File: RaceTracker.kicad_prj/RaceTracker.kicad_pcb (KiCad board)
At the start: 4 copper layers, 117 x 107.4 mm, 134 parts, among them J1 USB-C Sink, J10 MicroSD, J11 e-Paper (steckbar, Debug), J12 SWD-Programmierheader, J7 LiPo, Q1 2N7002, Q2 SIA817, Q3 2N7002, Q5 BSS138PS, U1 D21G18, U103 ZED-F9P RTK GNSS, U2 NINA-W102, U3 AP2112K-3.3 -> +3V3D, U5 BQ24195L, U6 AP2112K-3.3 -> +3V3, U7 MPU-6050 (I2C 0x68), Y1 32768Hz

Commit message: Routing: 93,8% automatisch via FreeRouting geroutet, Branding ergänzt
Specctra-DSN-Export der platzierten Platine → FreeRouting (Open-Source-
Autorouter, headless über kicad-cli/pcbnew-API-Pipeline) → SES-Re-Import.
20 Durchläufe, 388 → 24 unverdrahtete Verbindungen (93,8% Autoroute-Quote).
Verbleibende 24 sind größtenteils feinstufige QFN-Pins von U1 (SAMD21)
und U2 (NINA-W102) — brauchen manuelles Fine-Pitch-Routing, für das ich
ohne visuelle Kontrolle keine verlässliche automatische Lösung anbieten
kann.

Silkscreen-Branding auf der Rückseite ergänzt: Name "Jona Schramm -
Objectix Software Solutions" als Text sowie das Objectix-Logo, aus der
bereitgestellten PNG-Datei in ca. 440 gefüllte Silkscreen-Rechtecke
rasterisiert (0,15mm Zellgröße, 18x12mm) — plottet damit korrekt in
echte Fertigungs-Gerber-Dateien, anders als KiCads "Referenzbild"-
Funktion, die rein editor-intern bleibt.

Board auf 117x125mm erweitert (unterer Streifen für das Branding).

Verbleibende DRC-Meldungen (497, davon 29 unverdrahtet): größtenteils
Silkscreen-Kosmetik (Übersplitterung, Textgröße) ohne elektrische
Relevanz, plus dieselben ~5 Sub-Millimeter-Präzisionsartefakte aus der
bewährten Eagle-Spenderplatine wie zuvor dokumentiert.

Co-Authored-By: Claude Sonnet 5 <noreply@anthropic.com>
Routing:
- net GND: track 0.00 -> 720.4 mm, vias 0 -> 7
- net +3V3: track 0.00 -> 377.8 mm, vias 0 -> 13
- net I2C_SCL: track 0.00 -> 208.4 mm, vias 0 -> 9
- net I2C_SDA: track 0.00 -> 175.1 mm, vias 0 -> 6
- net SD_CS: track 0.00 -> 129.5 mm, vias 0 -> 4
- net LED_FIX: track 0.00 -> 127.2 mm, vias 0 -> 3
- net SPI_MOSI: track 0.00 -> 97.1 mm, vias 0 -> 1
- net EPD_RST: track 0.00 -> 96.8 mm, vias 0 -> 1
- net EPD_CS: track 0.00 -> 87.7 mm, vias 0 -> 2
- net Net-(U103-V_BKCP): track 0.00 -> 77.2 mm, vias 0 -> 2
- net IMU_INT: track 0.00 -> 76.6 mm, vias 0 -> 3
- net Net-(J10-DAT2): track 0.00 -> 72.9 mm, vias 0 -> 2
- net /Power/+3V8: track 0.00 -> 69.9 mm, vias 0 -> 6
- net SPI_MISO: track 0.00 -> 68.4 mm, vias 0 -> 3
- net Net-(U103-TIMEPULSE): track 0.00 -> 60.5 mm, vias 0 -> 2
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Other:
- board size 117 x 107.4 mm -> 117 x 125.4 mm
- board text added: "Design: Jona Schramm - Objectix Software Solutions"

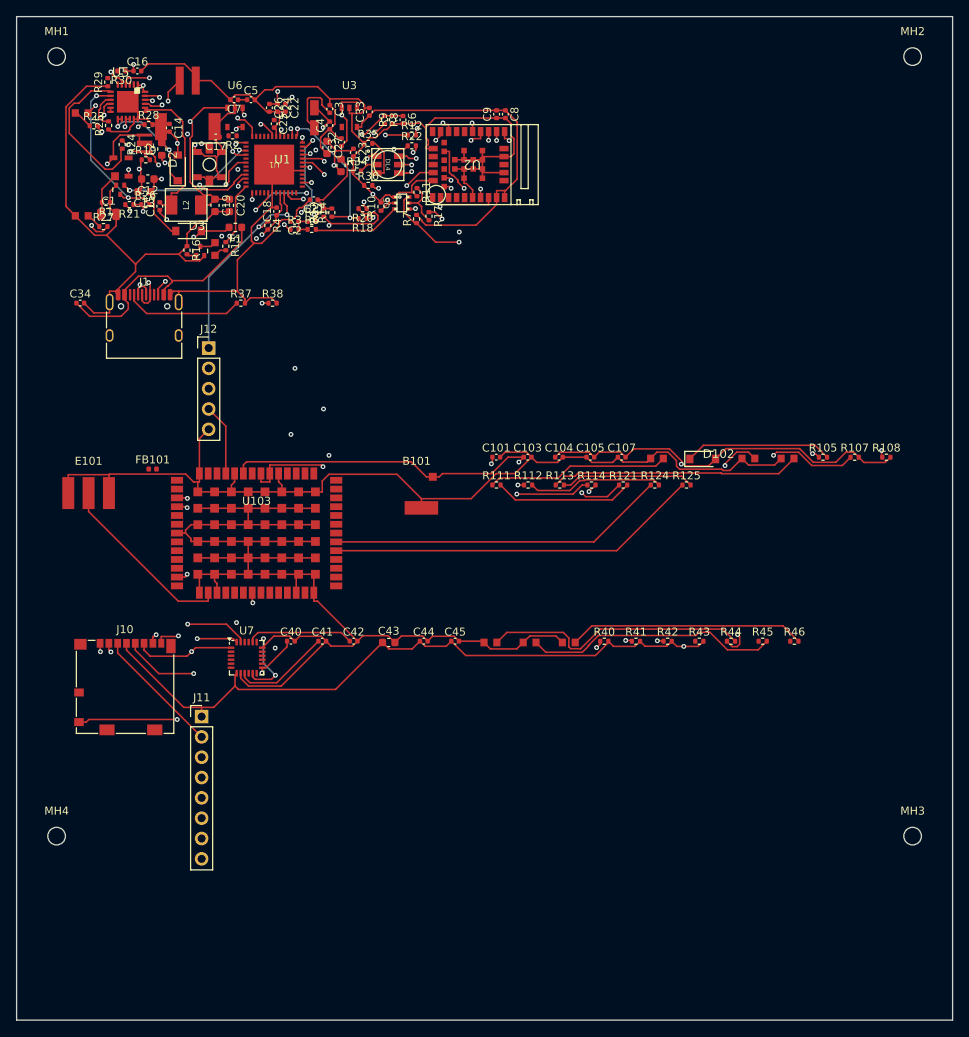
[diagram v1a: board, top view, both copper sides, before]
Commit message: PCB-Layout finalisiert: Edge-Connectoren, RF-Cluster restauriert, Routing 92,8%
- USB-C (J1), MicroSD (J10) und GPS-Antenne (E101) bündig an derselben
  Gehäusekante platziert, korrekt nach außen orientiert (90°, empirisch
  gegen pcbnew's CW-Rotationskonvention verifiziert). Akku-Stecker (J7)
  bleibt bewusst im Gehäuseinneren.
- GPS-RF-Cluster (E101/U103/FB101) nach versehentlicher manueller
  Verschiebung wieder auf die u-blox-Referenzabstände gebracht; Board
  wuchs dafür gezielt nur an der Oberkante (+15mm), keine Breitenzunahme.
- Fehlende Courtyard-Definition bei ZED_F9P_LGA102 ergänzt (verdeckte
  Überlappungen mit einem Dutzend Bauteilen, die DRC vorher nicht sah).
- Eagle-Import-Artefakte bereinigt: fehlplatzierte Ursprungsmarker auf
  8 Footprints (F.CrtYd -> F.Fab) behoben unclosed-courtyard-Fehler;
  verirrtes Mask-Polygon auf QFN48 behoben flächendeckende
  Solder-Mask-Bridge-Fehler zwischen allen Pin-Paaren.
  Solder_mask_margin auf beiden QFN-Footprints (48/24-Pin) auf 0 gesetzt,
  da 0.1016mm bei 0.5mm-Pitch die Maskenstege fast auflöste.
  Q2-Footprint (SON65P205X205X75-8N-MWSD): Pad-Größen leicht verkleinert,
  da einzelne Pads bei 0.65mm-Pitch 0mm Abstand hatten.
- Alle übrigen Platzierungskonflikte (Courtyard-Overlaps, Shorts durch
  Pad-Nähe) über iterativen Multi-Body-Relaxations-Solver aufgelöst.
- FreeRouting: 360/388 Netze (92,8%) automatisch geroutet, 4-lagig.
  Copper-edge-clearance-Regel auf 0.15mm gesetzt (realistischer Fab-Wert,
  vorher 0.5mm nicht erreichbar direkt an den bündigen Edge-Connectoren).
- Ergebnis: 0 DRC-Fehler (nur kosmetische Silk-Warnings), 0 ERC-Fehler,
  28 Netze für manuelles Routing offen.

Co-Authored-By: Claude Sonnet 5 <noreply@anthropic.com>
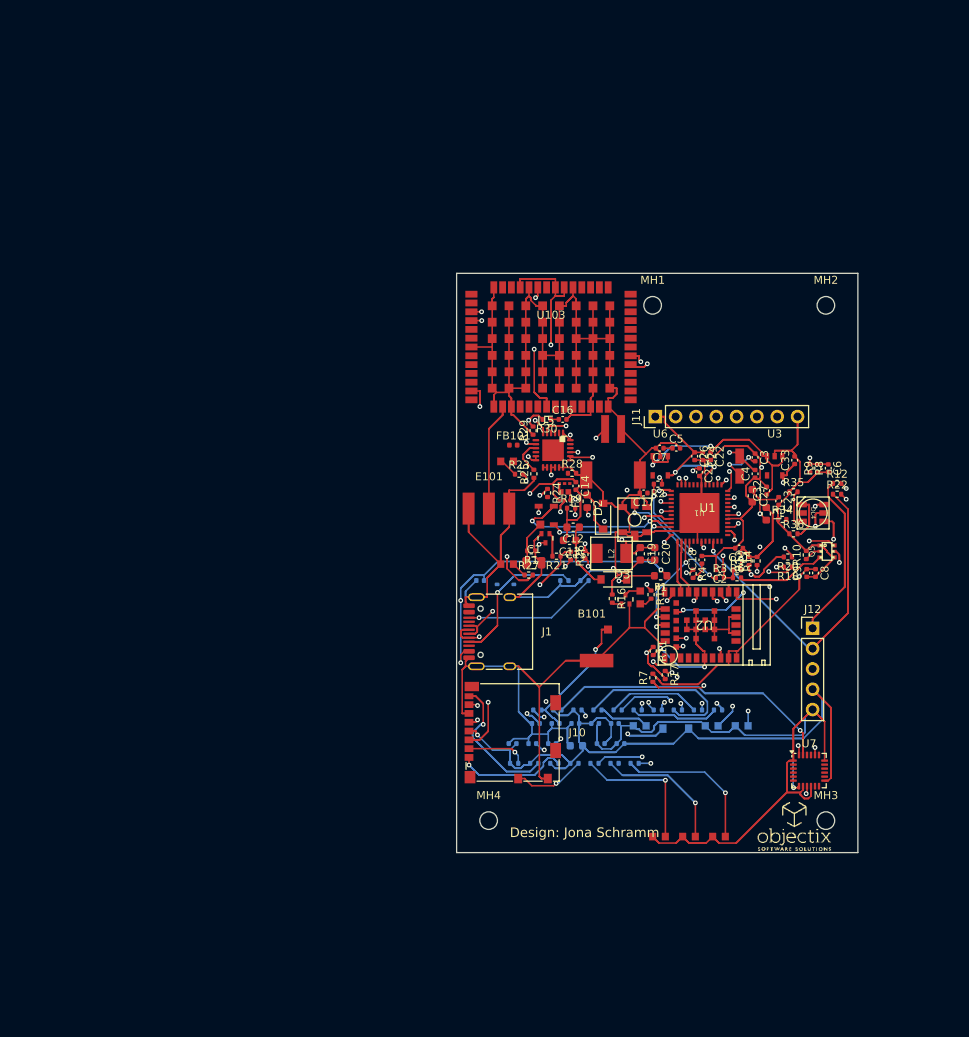
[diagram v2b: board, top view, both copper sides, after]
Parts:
- added D4: PESD5V0S1BA TVS VBUS, D_SOD-323, B.Cu at (61.1, 71.0)
- C101, C103, C104, C105, C107, C34, C40, C41, C43, C44, C45, D101, D102, D103, D104, R105, R107, R108, R111, R112, R113, R114, R121, R124, R125, R37, R38, R40, R41, R42, R43, R44, R45, R46: moved to B.Cu
- C42: value 2u2 (CPOUT) -> 2n2 (CPOUT); moved to B.Cu
- moved J12 83.2 mm to (99.5, 76.5)
- moved MH1 80.7 mm to (79.5, 36.1)
- moved U7 71.7 mm to (99.0, 94.2)
- moved C17 69.6 mm to (78.4, 59.6)
- moved PB1 69.3 mm to (77.3, 62.9)
- moved C8 69.2 mm to (99.9, 69.5)
- moved C9 69.2 mm to (98.8, 69.5)
- moved R21 69.2 mm to (67.5, 67.5)
- moved F2 69.0 mm to (71.3, 60.6)
- moved R26 68.9 mm to (69.3, 67.4), turned to -90 degrees
- moved C13 68.7 mm to (69.1, 65.5)
- moved C7 68.7 mm to (80.4, 53.9)
- moved R19 68.7 mm to (69.3, 61.4)
- moved R24 68.7 mm to (66.4, 59.5)
- moved C1 68.7 mm to (64.7, 68.3)
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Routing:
- net GND: track 720.4 -> 820.4 mm, vias 7 -> 4
- net EPD_RST: track 96.8 -> 0.00 mm, vias 1 -> 0
- net EPD_CS: track 87.7 -> 0.00 mm, vias 2 -> 0
- net LED_ERR: track 0.00 -> 82.6 mm, vias 0 -> 2
- net IMU_INT: track 76.6 -> 0.00 mm, vias 3 -> 0
- net Net-(U1-PA13): track 0.00 -> 72.8 mm, vias 0 -> 2
- net SPI_SCK: track 20.4 -> 89.5 mm, vias 1 -> 2
- net Net-(U103-V_RF): track 50.3 -> 116.0 mm
- net /MCU_Radio/SWD_NRESET: track 0.00 -> 62.9 mm, vias 0 -> 2
- net LED_FIX: track 127.2 -> 66.3 mm, vias 3 -> 2
- net I2C_SDA: track 175.1 -> 228.4 mm, vias 6 -> 7
- net Net-(U7-REGOUT): track 12.2 -> 65.3 mm, vias 0 -> 2
- net Net-(U103-RTK_STAT): track 42.3 -> 93.1 mm, vias 0 -> 2
- net /MCU_Radio/PA14_S2_RTS/CS: track 0.00 -> 50.2 mm, vias 0 -> 3
- net Net-(Q5B-G): track 6.19 -> 55.6 mm, vias 0 -> 2
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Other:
- board size 117 x 125.4 mm -> 50.2 x 72.4 mm
- board text added: "Design: Jona Schramm"
- board text removed: "Design: Jona Schramm - Objectix Software Solutions"
